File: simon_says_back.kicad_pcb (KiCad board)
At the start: 2 copper layers, 97 x 60 mm, 4 parts

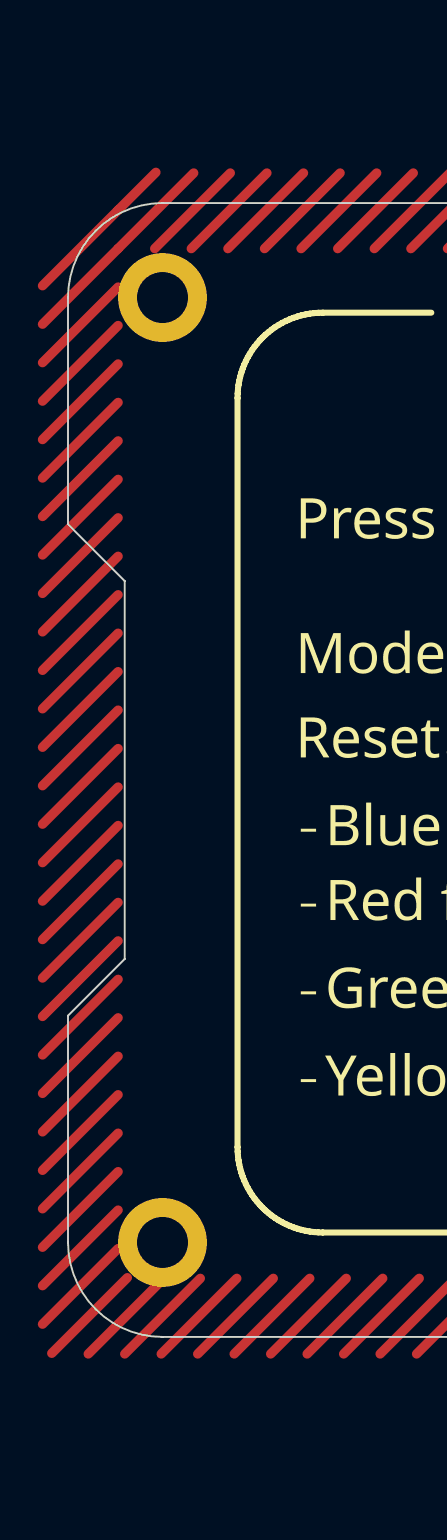
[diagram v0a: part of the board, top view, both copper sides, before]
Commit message: Added order number placeholder
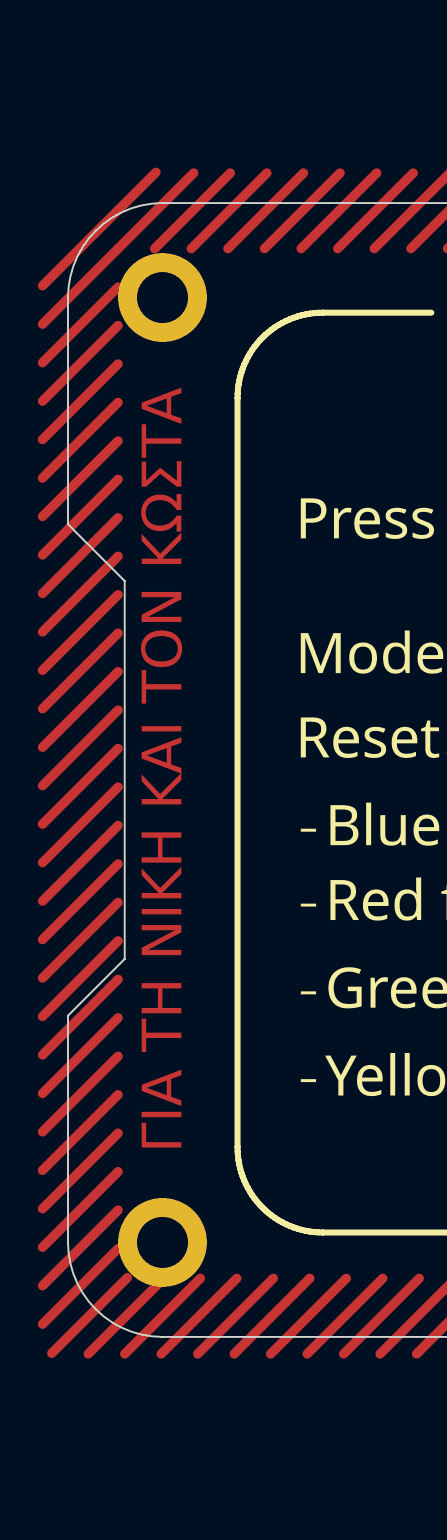
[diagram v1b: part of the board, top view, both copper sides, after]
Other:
- board text added: "JLCJLCJLCJLC"
- board text added: "ΓΙΑ ΤΗ ΝΙΚΗ ΚΑΙ ΤΟΝ ΚΩΣΤΑ"
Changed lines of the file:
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@@
   (gr_line (start 147 55) (end 147 67)
     (stroke (width 0.1) (type default)) (layer "Edge.Cuts"))
+  (gr_text "ΓΙΑ ΤΗ ΝΙΚΗ ΚΑΙ ΤΟΝ ΚΩΣΤΑ" (at 55.025 80 90) (layer "F.Cu")
+    (effects (font (size 2.1 2.1) (thickness 0.32)))
+  )
+  (gr_text "JLCJLCJLCJLC" (at 99.825 100.5) (layer "B.SilkS")
+    (effects (font (size 1.5 1.5) (thickness 0.2)) (justify mirror))
+  )
   (group "" (id 65ebed86-901c-4b5e-ac89-c092589016e3)
     (members
